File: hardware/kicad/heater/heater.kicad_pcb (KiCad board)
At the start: 2 copper layers, 56 x 56 mm, 2 parts, among them J1 Heater and NTC leads

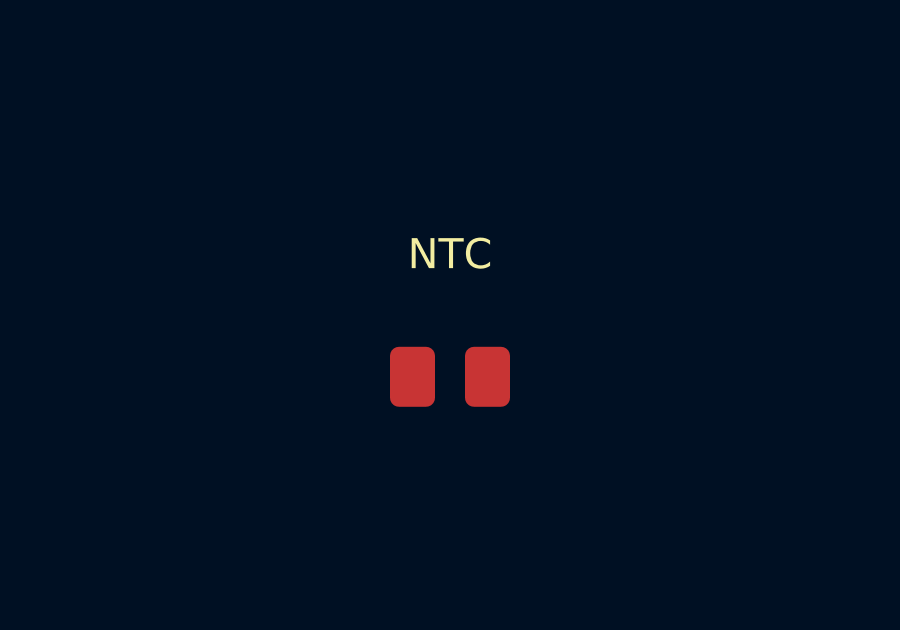
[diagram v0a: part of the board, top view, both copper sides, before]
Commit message: Resize heater NTC pads to standard 0603 land
JLCPCB flexible heater "Solder NTC" requires reserved pads. Shrink the
center NTC footprint from a generic 1.5x2 mm pair at 2.5 mm pitch to a
standard 0603 reflow land (0.9x1.0 mm at 1.65 mm pitch) so JLC can
solder a 0603 NTC at the heater center. Regenerate the Gerber zip.

Co-Authored-By: Claude Opus 4.7 (1M context) <noreply@anthropic.com>
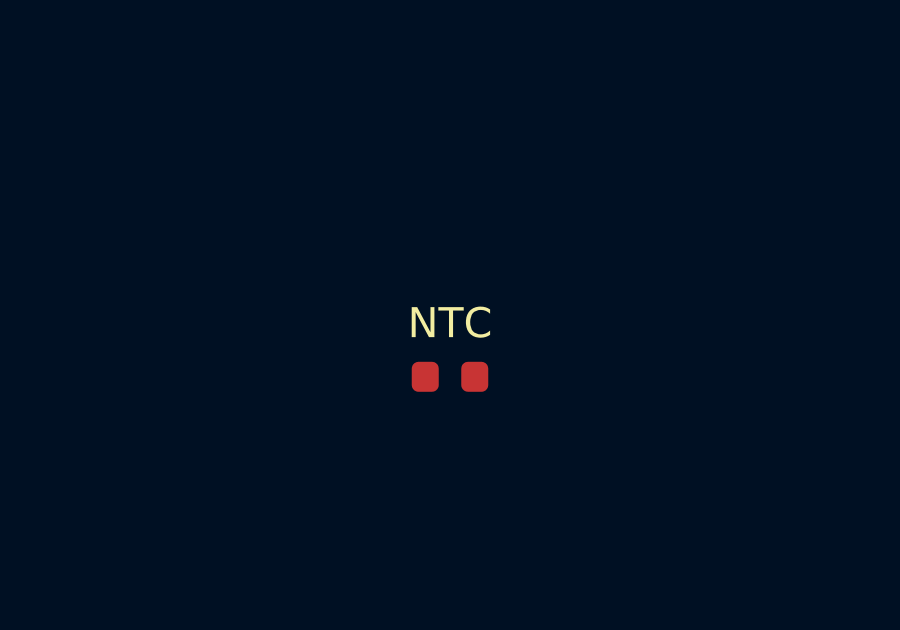
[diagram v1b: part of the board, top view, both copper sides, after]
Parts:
- NTC1: value 100k NTC requested -> 100k NTC 0603

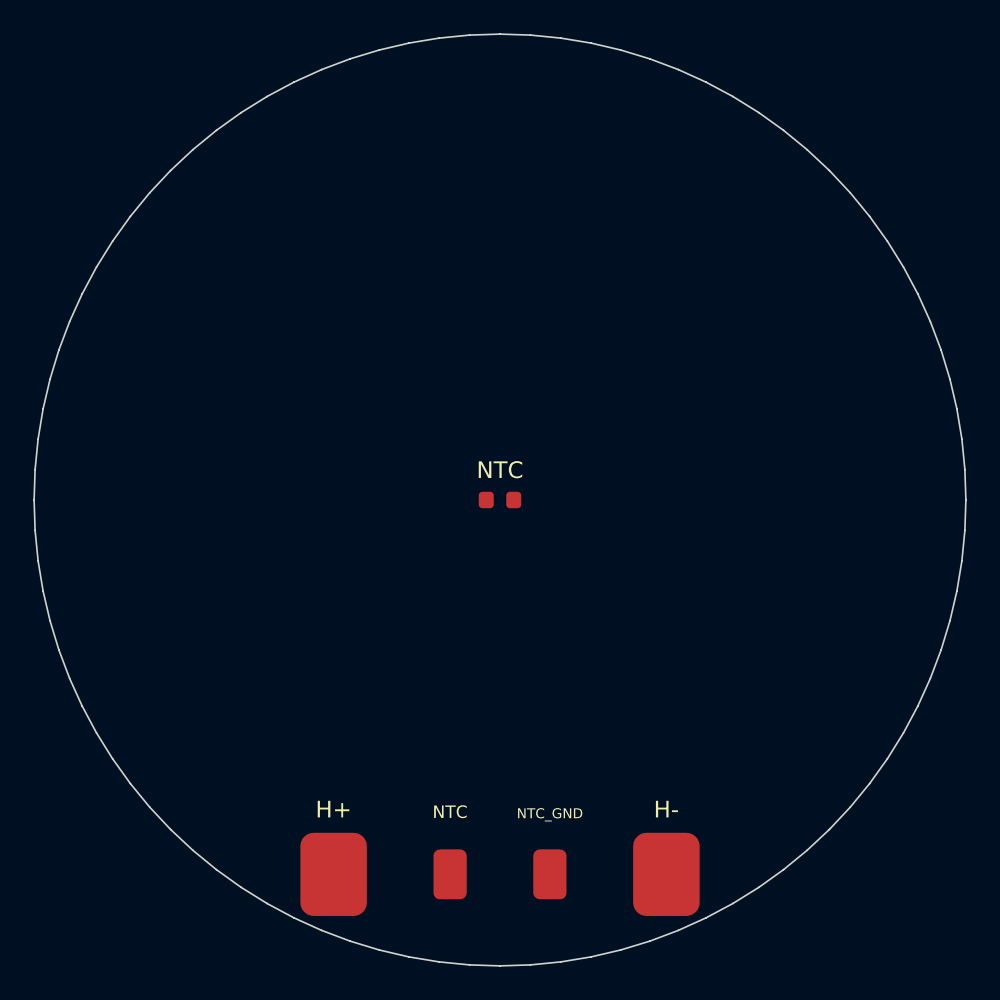
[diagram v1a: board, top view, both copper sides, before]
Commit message: Resize flexible heater to Ø55 and fix size/resistance docs
Heater outline was Ø56 "to match the control PCB", but the control PCB
was resized to Ø50. Re-base the heater on the thermal stack instead:
Ø55 covers the aluminum spreader (Ø54.5), seats on the bottom-tray
heater-seat step (Ø50.7/Ø57.2), and stays under the cup contact pad
(Ø56.5). Reconcile the heater resistance to 12Ω (12V/1A/12W) across all
docs; the Open Items "15Ω provisional" note contradicted §3, the heater
README, and the R3/Q1 continuous-1A assumptions.

- generate_heater.py: OUTLINE_RADIUS 28.0 -> 27.5; drop "matches PCB"
  rationale in board comment and README, regenerate PCB/README/gerbers/zip
- design-notes.md: heater final resistance 15Ω -> 12Ω
- mechanical/README.md: split stale "PCB/heater OD 56mm" into PCB Ø50 +
  flexible heater Ø55

Co-Authored-By: Claude Opus 4.8 (1M context) <noreply@anthropic.com>
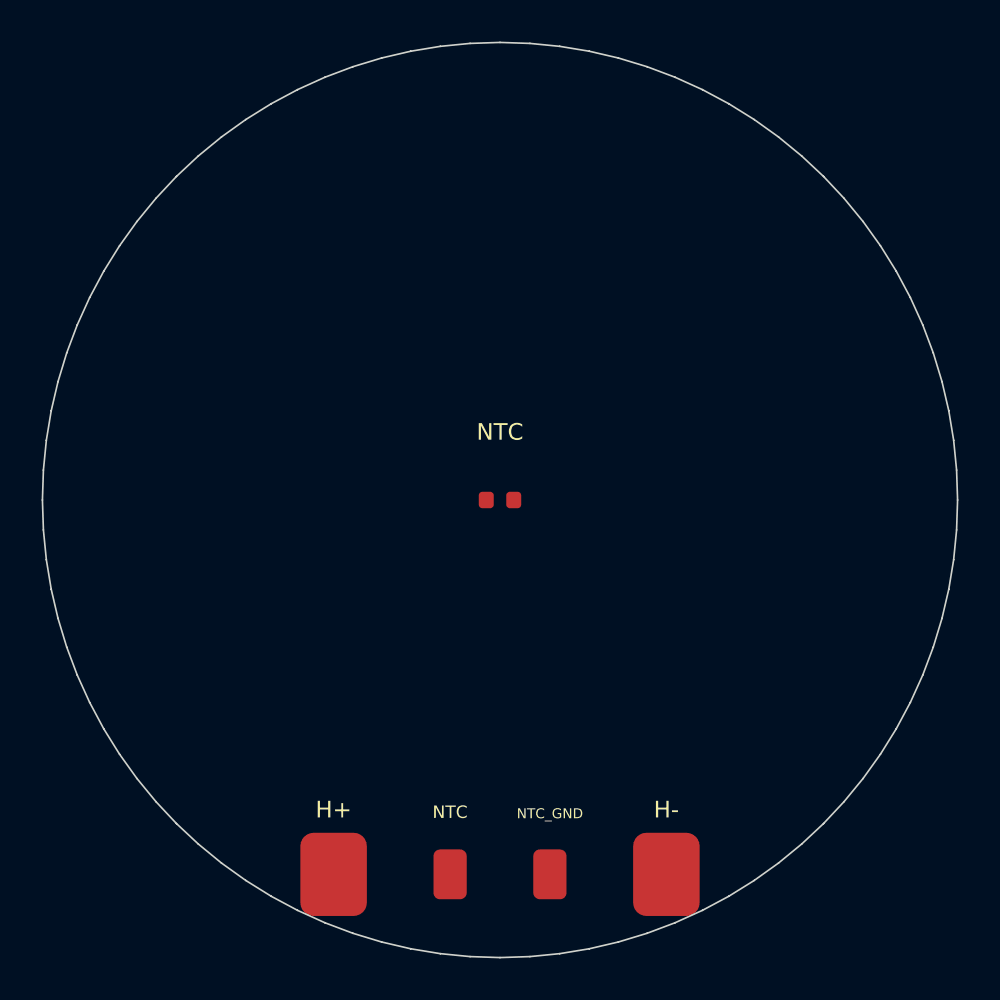
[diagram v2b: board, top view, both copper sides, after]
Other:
- board size 56 x 56 mm -> 55 x 55 mm

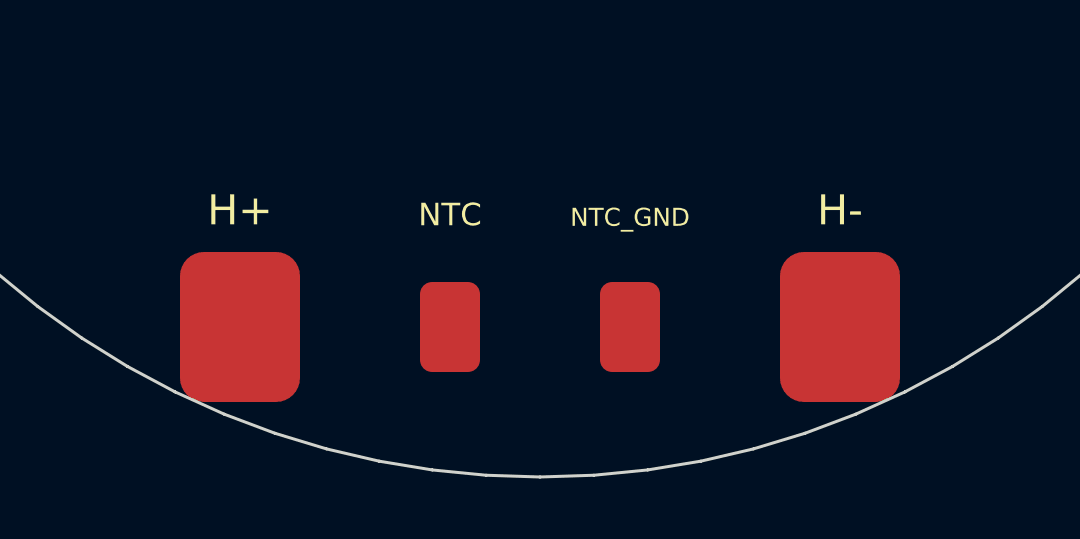
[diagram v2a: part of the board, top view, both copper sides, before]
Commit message: Move heater leadout pads inward and regen gerbers
J1 leadout footprint moved Y122.5 -> 121.7 (0.8mm toward center).
Regenerate gerbers/zip from the hand-edited PCB and sync the leadout
position in generate_heater.py so a future regen keeps the move.

Co-Authored-By: Claude Opus 4.8 (1M context) <noreply@anthropic.com>
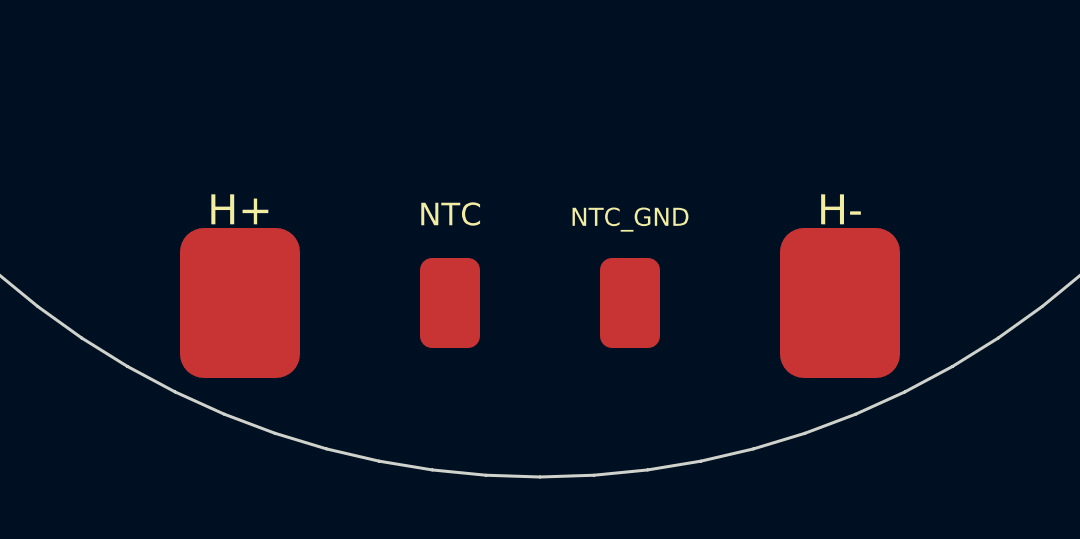
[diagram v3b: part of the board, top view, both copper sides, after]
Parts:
- moved J1 0.80 mm to (100.0, 121.7)
